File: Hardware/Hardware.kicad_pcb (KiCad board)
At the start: 4 copper layers, 55.5 x 29 mm, 52 parts, among them J1 Conn_01x04, J2 Conn_Coaxial, J3 USB_C_Receptacle_USB2.0_16P, J4 Conn_01x04, Q1 MMBT2222A, SW1 SW_Push, U1 STM32WB55RGVx, U2 USBLC6-2SC6, U3 MIC5365-3.3YD5, U4 BME280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

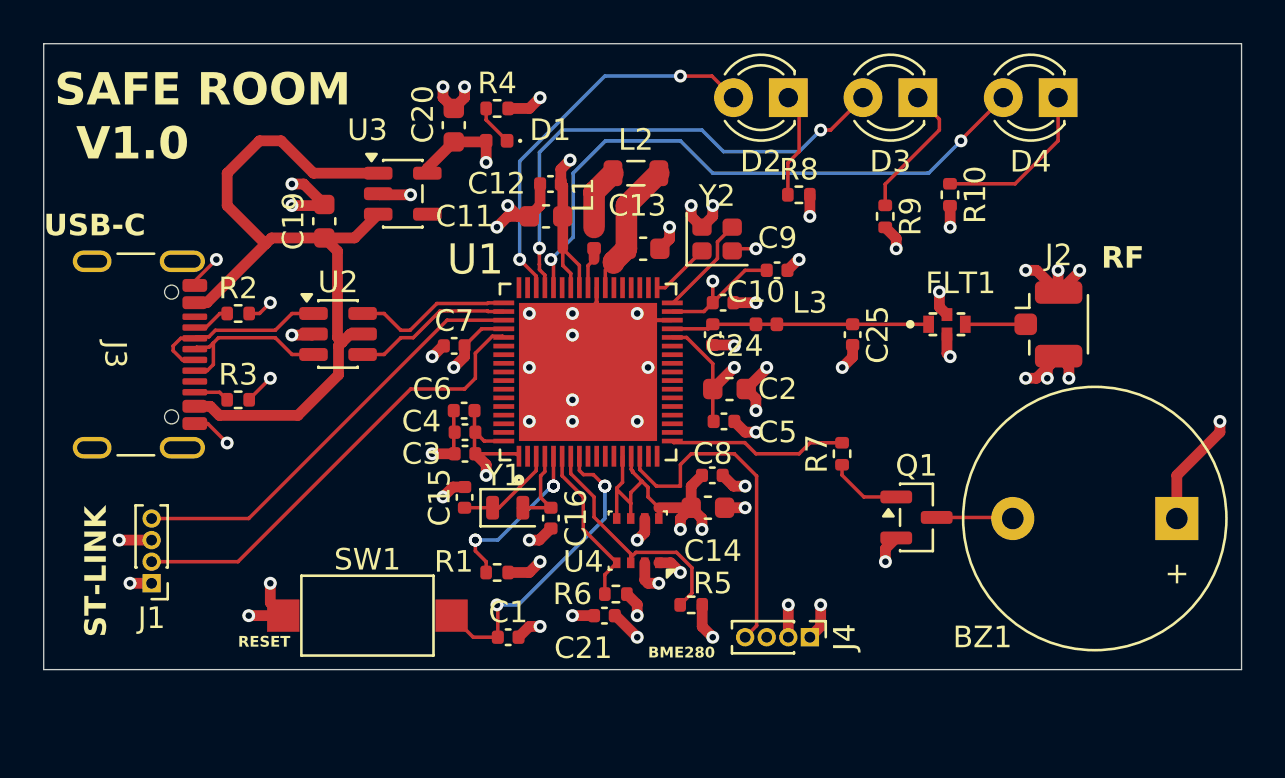
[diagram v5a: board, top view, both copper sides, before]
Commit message: [CORRECCTION DU PCB] : J'ai corrigé le PCB après avoir discuter avec le Fabricant PCB Way, j'ai corrigé le footprint de la capacité C14 avec ce qui correspond à ce qui est vendu par mouser electronics. Le bon footprint est 0402_1005. J'ai également corrigé le footprint des connecteurs 01x04 avec un footprint de 2.54mm. Avant c'était 1mm, du coup j'ai modifié le PCB. J'ai également modifier le placement des capacité et des inductances, plus proche du stm32.
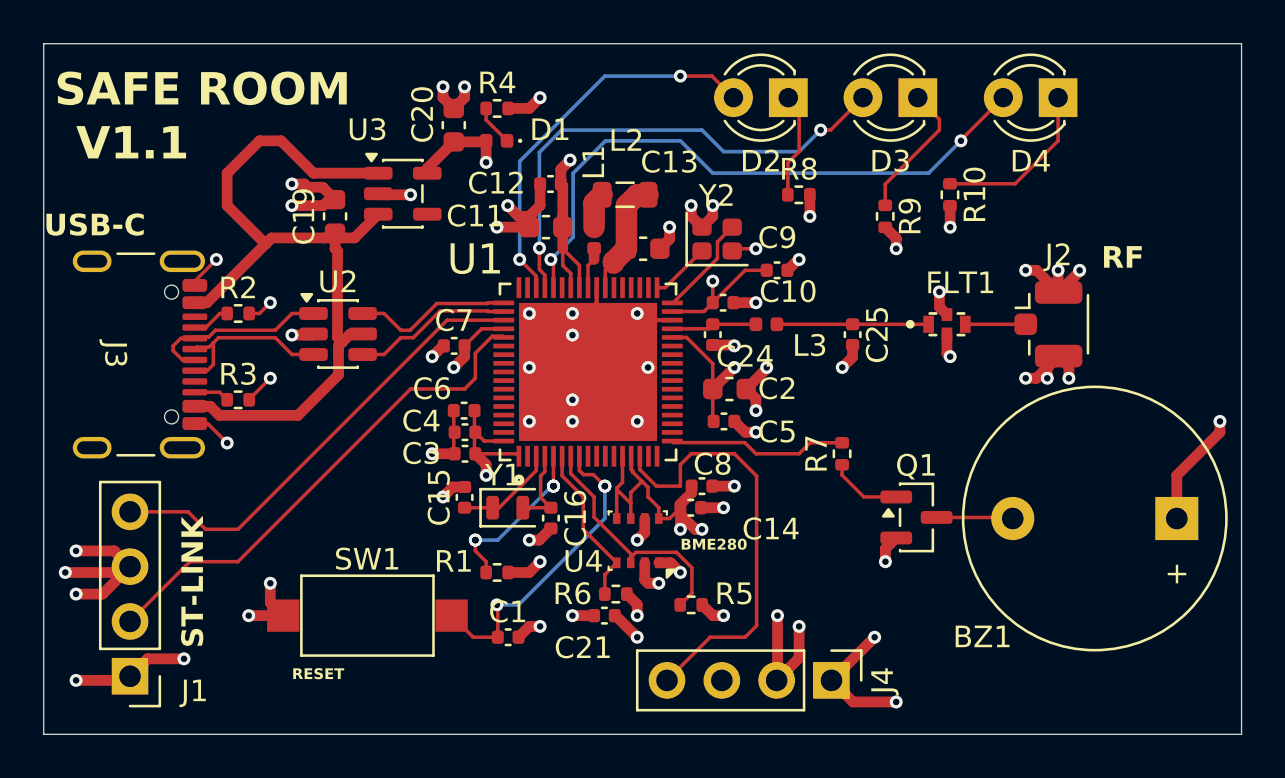
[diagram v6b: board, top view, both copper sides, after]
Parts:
- C14: footprint Capacitor_SMD:C_0603_1608Metric -> Capacitor_SMD:C_0402_1005Metric
- J1, J4: footprint Connector_PinHeader_1.00mm:PinHeader_1x04_P1.00mm_Vertical -> Connector_PinHeader_2.54mm:PinHeader_1x04_P2.54mm_Vertical
- moved J1 4.42 mm to (133.5, 85.8)
- moved J4 2.24 mm to (166.0, 86.0)
- moved L2 1.12 mm to (156.4, 63.5)
- moved C14 0.80 mm to (159.5, 78.0)
- moved C8 0.69 mm to (160.0, 77.0)
- moved C19 0.55 mm to (143.0, 64.5)
- moved C11 0.50 mm to (152.8, 65.0)
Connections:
- C25 pad 1: /RF -> Net-(FLT1-IN)
- FLT1 pad 1: /RF -> Net-(FLT1-IN)
- L3 pad 2: /RF -> Net-(FLT1-IN)
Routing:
- net GND: track 74.3 -> 87.1 mm, vias 61 -> 64
- net /RF: track 12.0 -> 3.96 mm
- net +3V3: track 64.0 -> 71.8 mm, vias 15 -> 17
- net Net-(FLT1-IN): track 0.00 -> 7.03 mm
- net /MQ2_sensor: track 15.7 -> 20.1 mm
- net /SWDCLK: track 21.3 -> 23.5 mm
- net /SWDIO: track 20.1 -> 21.7 mm
- net Net-(L1-Pad2): track 2.88 -> 1.67 mm
- net Net-(U1-VFBSMPS): track 5.86 -> 4.95 mm
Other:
- board size 55.5 x 29 mm -> 55.5 x 32 mm
- board text added: "MADE BY KAMDA TEZEBO"
- board text added: "V1.1"
- board text removed: "DESIGNER PAR KAMDA TEZEBO"
- board text removed: "V1.0"

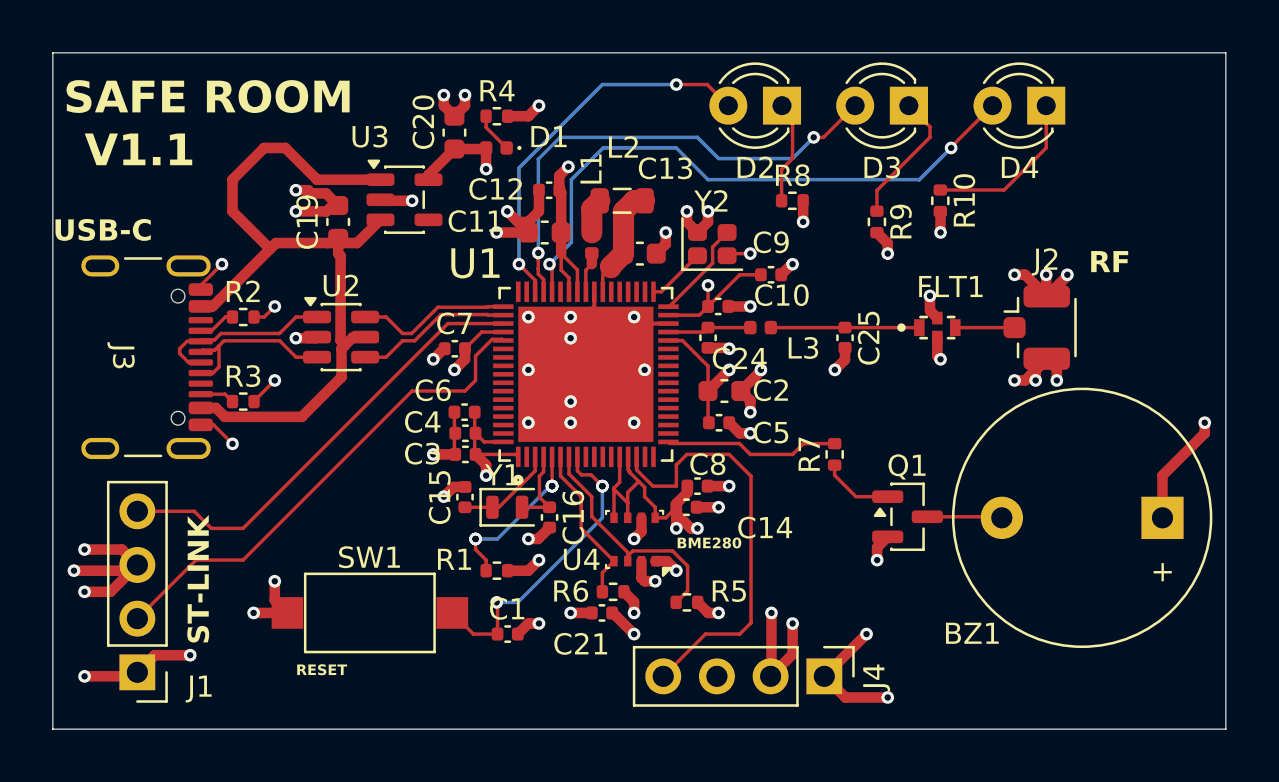
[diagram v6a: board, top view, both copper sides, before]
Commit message: [MOD] : Changement de l'empreinte des connecteurs 01x04 pour celui de 2.54mm, et adjustement de la schématique du RF
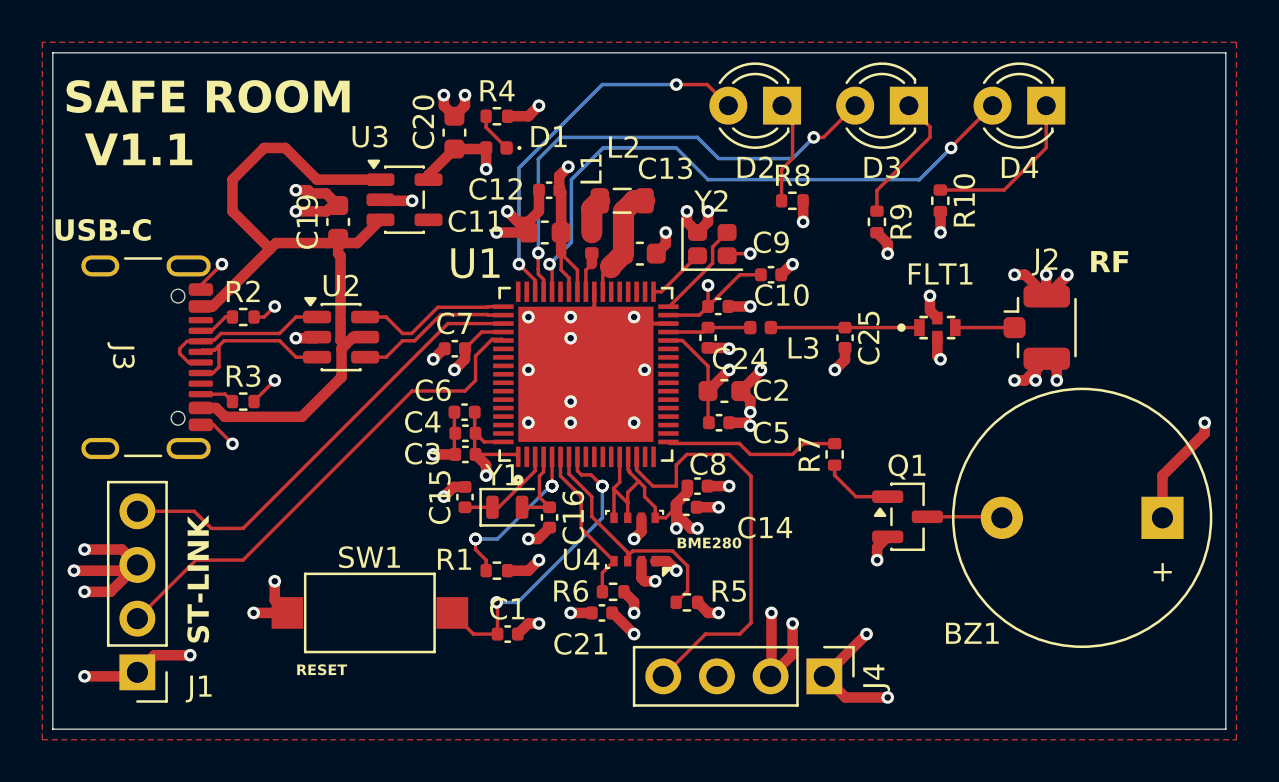
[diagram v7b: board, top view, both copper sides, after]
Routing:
- added copper zone on F.Cu, net GND
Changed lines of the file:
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@@
 			(pdf_back_fp_property_popups yes)
 			(pdf_metadata yes)
-			(pdf_single_document yes)
+			(pdf_single_document no)
 			(dxfpolygonmode yes)
 			(dxfimperialunits yes)
@@
 			(crossoutdnponfab yes)
 			(subtractmaskfromsilk no)
-			(outputformat 4)
+			(outputformat 1)
 			(mirror no)
 			(drillshape 0)
 			(scaleselection 1)
-			(outputdirectory "Manufacturing/")
+			(outputdirectory "C:/Users/admin/Desktop/Project/Hardware/Manufacturing/v2/geber/")
 		)
 	)
@@
 		(at 171.35 69.5)
 		(property "Reference" "FLT1"
-			(at 0.63553 -1.90656 0)
+			(at 0.15 -2.5 0)
 			(layer "F.SilkS")
 			(effects
@@
 	)
 	(segment
+		(start 162.355597 74)
+		(end 162.5 74.144403)
+		(width 0.5)
+		(layer "F.Cu")
+		(net 4)
+	)
+	(segment
 		(start 141.95 70)
 		(end 142 69.95)
@@
 	)
 	(segment
-		(start 162 74.5)
-		(end 161.5 74)
-		(width 0.5)
-		(layer "F.Cu")
-		(net 4)
-	)
-	(segment
 		(start 147.5 71)
 		(end 148 70.5)
@@
 	)
 	(segment
-		(start 162.5 74.5)
-		(end 162 74.5)
-		(width 0.5)
-		(layer "F.Cu")
-		(net 4)
-	)
-	(segment
 		(start 163 71.55)
 		(end 162.05 72.5)
@@
 	)
 	(segment
+		(start 161.5 74)
+		(end 162.355597 74)
+		(width 0.5)
+		(layer "F.Cu")
+		(net 4)
+	)
+	(segment
 		(start 152 81)
 		(end 152.5 80.5)
@@
 	)
 	(via
-		(at 162.5 74.5)
+		(at 162.5 74.144403)
 		(size 0.6)
 		(drill 0.3)
@@
 	)
 	(zone
+		(net 4)
+		(net_name "GND")
+		(layer "F.Cu")
+		(hatch edge 0.5)
+		(priority 2)
+		(connect_pads
+			(clearance 0.3)
+		)
+		(min_thickness 0.25)
+		(filled_areas_thickness no)
+		(fill yes
+			(thermal_gap 0.5)
+			(thermal_bridge_width 0.5)
+		)
+		(polygon
+			(pts
+				(xy 129 56) (xy 129 89) (xy 185.5 89) (xy 185.5 56)
+			)
+		)
+	)
+	(zone
